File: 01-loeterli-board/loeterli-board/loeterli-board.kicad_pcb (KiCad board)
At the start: 2 copper layers, 100 x 60 mm, 45 parts, among them J5 Screw_Terminal_01x03, J8 Conn_01x03, Q1 PSMN5R2-60YL, SW1 SW_Push, SW2 SW_Push, SW3 SW_Push, SW4 SW_Push, U1 VOM1271T, U2 STM32F103C8Tx, U3 R-78HB3.3-0.5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

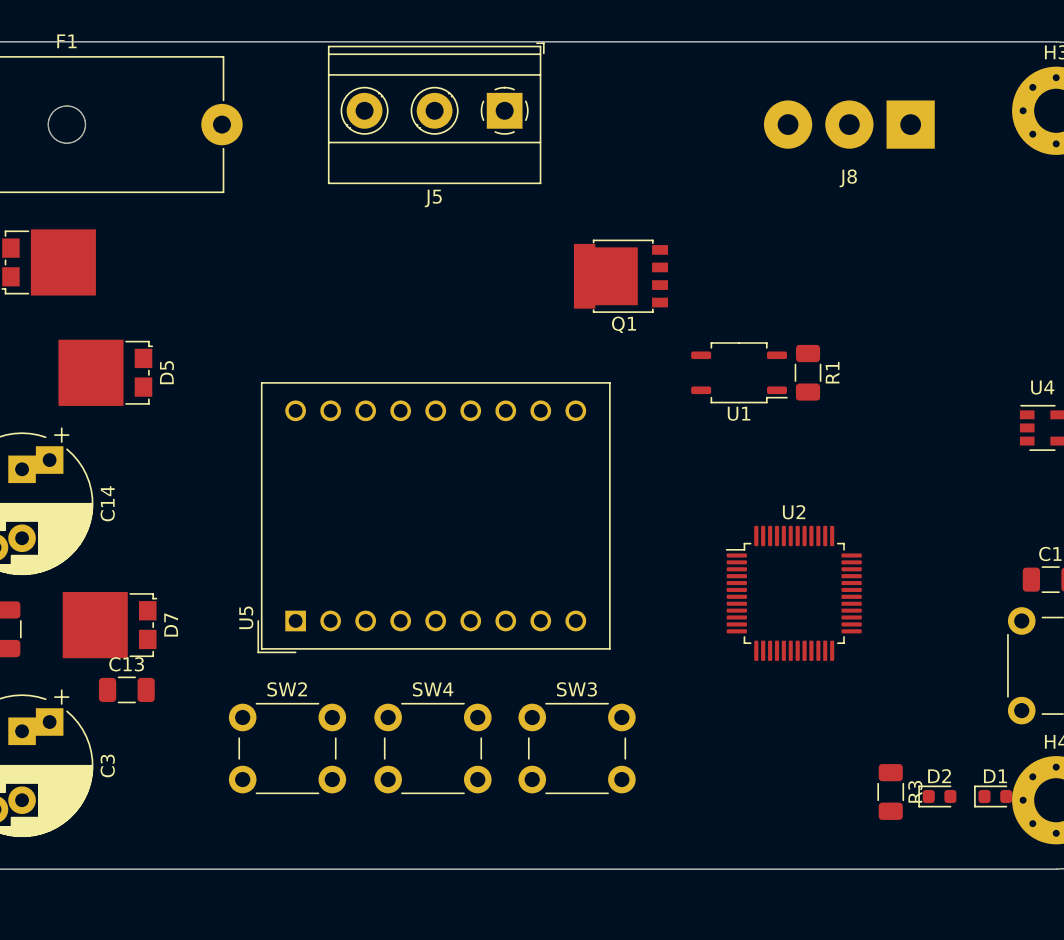
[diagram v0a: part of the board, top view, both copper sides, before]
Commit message: added readme image + misc
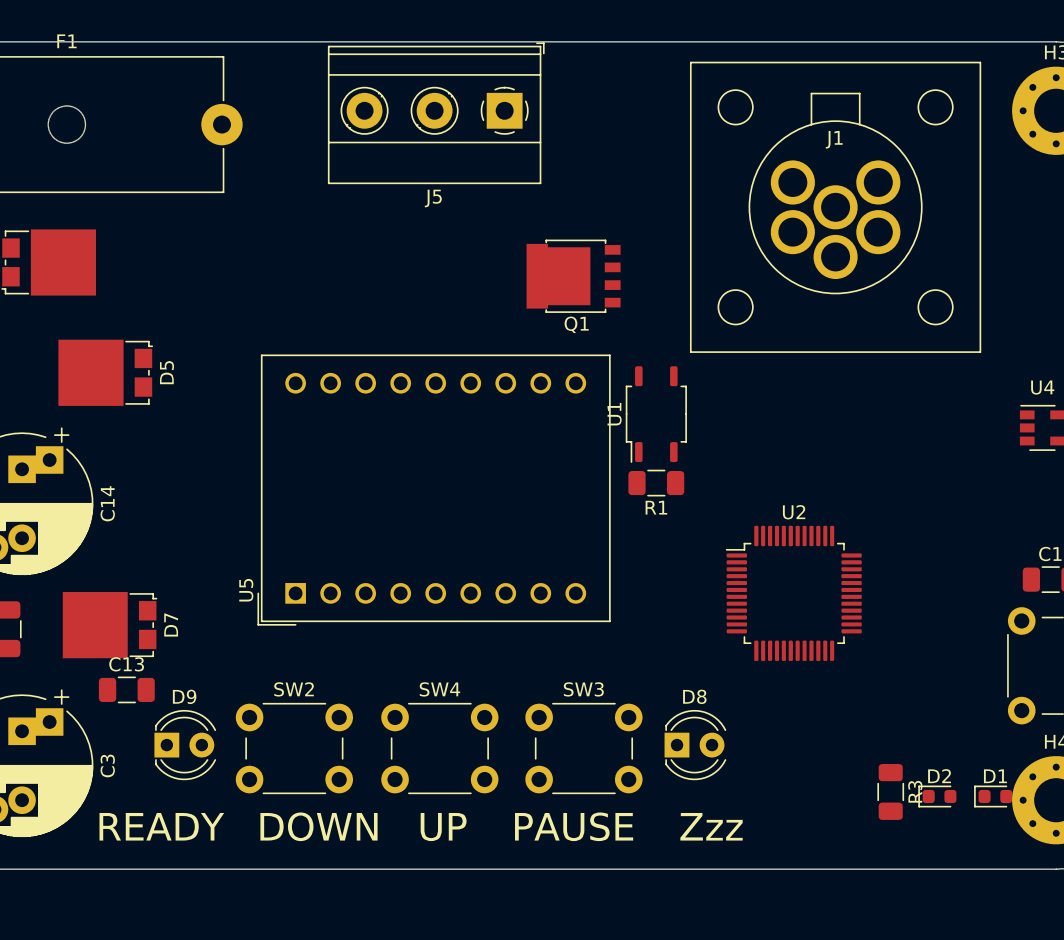
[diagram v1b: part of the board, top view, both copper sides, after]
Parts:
- removed J8: Conn_01x03, Connector_Wire:SolderWirePad_1x03_P4.445mm_Drill1.5mm
- added D8: LED, LED_THT:LED_D4.0mm, F.Cu at (187.5, 101.0)
- added D9: LED, LED_THT:LED_D4.0mm, F.Cu at (150.5, 101.0)
- added J1: RPC1-12RB-6P, loeterli:RPC1-12RB-6P, F.Cu at (199.0, 62.0)
- moved R1 13.6 mm to (186.0, 82.0), turned to 180 degrees
- moved U1 6.71 mm to (186.0, 77.0), turned to 90 degrees
- moved Q1 3.44 mm to (180.0, 67.0)
- moved U5 2.00 mm to (159.8, 90.0)
- moved SW2 0.50 mm to (156.5, 99.0)
- moved SW3 0.50 mm to (177.5, 99.0)
- moved SW4 0.50 mm to (167.1, 99.0)
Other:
- board text added: "DOWN"
- board text added: "PAUSE"
- board text added: "READY"
- board text added: "UP"
- board text added: "Zzz"

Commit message: misc
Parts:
- added D10: D, Diode_SMD:D_0603_1608Metric, F.Cu at (215.0, 119.5)
- added R7: 100k, Resistor_SMD:R_1206_3216Metric, F.Cu at (215.8, 116.6)
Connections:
- J1 pad 1: Net-(J1-Pad1) -> Earth
- J1 pad 2: Net-(J1-Pad2) -> GND
- J1 pad 5: Net-(J1-Pad5) -> H+
- Q1 pad 1: Net-(Q1-Pad1) -> H+
- Q1 pad 2: Net-(Q1-Pad1) -> H+
- Q1 pad 3: Net-(Q1-Pad1) -> H+
- U1 pad 3: Net-(Q1-Pad1) -> H+
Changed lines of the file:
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@@
     (tracks 0)
     (zones 0)
-    (modules 47)
-    (nets 91)
+    (modules 49)
+    (nets 89)
   )
   (page A4)
@@
   (net 78 V_RECT)
   (net 79 AC_N)
-  (net 80 "Net-(Q1-Pad1)")
-  (net 81 "Net-(J1-Pad3)")
-  (net 82 "Net-(J1-Pad6)")
-  (net 83 "Net-(J1-Pad5)")
-  (net 84 "Net-(J1-Pad4)")
-  (net 85 "Net-(J1-Pad2)")
-  (net 86 "Net-(J1-Pad1)")
-  (net 87 "Net-(D8-Pad2)")
-  (net 88 "Net-(D8-Pad1)")
-  (net 89 "Net-(D9-Pad2)")
-  (net 90 "Net-(D9-Pad1)")
+  (net 80 "Net-(J1-Pad3)")
+  (net 81 "Net-(J1-Pad6)")
+  (net 82 "Net-(J1-Pad4)")
+  (net 83 "Net-(D8-Pad2)")
+  (net 84 "Net-(D8-Pad1)")
+  (net 85 "Net-(D9-Pad2)")
+  (net 86 "Net-(D9-Pad1)")
+  (net 87 ZCD)
+  (net 88 H+)
   (net_class Default "This is the default net class."
     (clearance 0.2)
@@
     (add_net Earth)
     (add_net GND)
+    (add_net H+)
     (add_net "Net-(C1-Pad1)")
     (add_net "Net-(C11-Pad1)")
@@
     (add_net "Net-(D9-Pad2)")
     (add_net "Net-(F1-Pad2)")
-    (add_net "Net-(J1-Pad1)")
-    (add_net "Net-(J1-Pad2)")
     (add_net "Net-(J1-Pad3)")
     (add_net "Net-(J1-Pad4)")
-    (add_net "Net-(J1-Pad5)")
     (add_net "Net-(J1-Pad6)")
-    (add_net "Net-(Q1-Pad1)")
     (add_net "Net-(Q1-Pad4)")
     (add_net "Net-(R1-Pad2)")
@@
     (add_net TEMP)
     (add_net V_RECT)
+    (add_net ZCD)
     (add_net nGATE)
+  )
+  (module Resistor_SMD:R_1206_3216Metric (layer F.Cu)
+    (at 215.76 116.56)
+    (descr "Resistor SMD 1206 (3216 Metric), square (rectangular) end terminal, IPC_7351 nominal, (Body size source: http://www.tortai-tech.com/upload/download/2011102023233369053.pdf), generated with kicad-footprint-generator")
+    (tags resistor)
+    (attr smd)
+    (fp_text reference R7 (at 0 -1.82) (layer F.SilkS)
+      (effects (font (size 1 1) (thickness 0.15)))
+    )
+    (fp_text value 100k (at 0 1.82) (layer F.Fab)
+      (effects (font (size 1 1) (thickness 0.15)))
+    )
+    (fp_text user %R (at 0 0) (layer F.Fab)
+      (effects (font (size 0.8 0.8) (thickness 0.12)))
+    )
+    (fp_line (start 2.28 1.12) (end -2.28 1.12) (layer F.CrtYd) (width 0.05))
+    (fp_line (start 2.28 -1.12) (end 2.28 1.12) (layer F.CrtYd) (width 0.05))
+    (fp_line (start -2.28 -1.12) (end 2.28 -1.12) (layer F.CrtYd) (width 0.05))
+    (fp_line (start -2.28 1.12) (end -2.28 -1.12) (layer F.CrtYd) (width 0.05))
+    (fp_line (start -0.602064 0.91) (end 0.602064 0.91) (layer F.SilkS) (width 0.12))
+    (fp_line (start -0.602064 -0.91) (end 0.602064 -0.91) (layer F.SilkS) (width 0.12))
+    (fp_line (start 1.6 0.8) (end -1.6 0.8) (layer F.Fab) (width 0.1))
+    (fp_line (start 1.6 -0.8) (end 1.6 0.8) (layer F.Fab) (width 0.1))
+    (fp_line (start -1.6 -0.8) (end 1.6 -0.8) (layer F.Fab) (width 0.1))
+    (fp_line (start -1.6 0.8) (end -1.6 -0.8) (layer F.Fab) (width 0.1))
+    (pad 2 smd roundrect (at 1.4 0) (size 1.25 1.75) (layers F.Cu F.Paste F.Mask) (roundrect_rratio 0.2)
+      (net 87 ZCD))
+    (pad 1 smd roundrect (at -1.4 0) (size 1.25 1.75) (layers F.Cu F.Paste F.Mask) (roundrect_rratio 0.2)
+      (net 78 V_RECT))
+    (model ${KISYS3DMOD}/Resistor_SMD.3dshapes/R_1206_3216Metric.wrl
+      (at (xyz 0 0 0))
+      (scale (xyz 1 1 1))
+      (rotate (xyz 0 0 0))
+    )
+  )
+  (module Diode_SMD:D_0603_1608Metric (layer F.Cu)
+    (at 215 119.5)
+    (descr "Diode SMD 0603 (1608 Metric), square (rectangular) end terminal, IPC_7351 nominal, (Body size source: http://www.tortai-tech.com/upload/download/2011102023233369053.pdf), generated with kicad-footprint-generator")
+    (tags diode)
+    (attr smd)
+    (fp_text reference D10 (at 0 -1.43) (layer F.SilkS)
+      (effects (font (size 1 1) (thickness 0.15)))
+    )
+    (fp_text value D (at 0 1.43) (layer F.Fab)
+      (effects (font (size 1 1) (thickness 0.15)))
+    )
+    (fp_text user %R (at 0 0) (layer F.Fab)
+      (effects (font (size 0.4 0.4) (thickness 0.06)))
+    )
+    (fp_line (start 1.48 0.73) (end -1.48 0.73) (layer F.CrtYd) (width 0.05))
+    (fp_line (start 1.48 -0.73) (end 1.48 0.73) (layer F.CrtYd) (width 0.05))
+    (fp_line (start -1.48 -0.73) (end 1.48 -0.73) (layer F.CrtYd) (width 0.05))
+    (fp_line (start -1.48 0.73) (end -1.48 -0.73) (layer F.CrtYd) (width 0.05))
+    (fp_line (start -1.485 0.735) (end 0.8 0.735) (layer F.SilkS) (width 0.12))
+    (fp_line (start -1.485 -0.735) (end -1.485 0.735) (layer F.SilkS) (width 0.12))
+    (fp_line (start 0.8 -0.735) (end -1.485 -0.735) (layer F.SilkS) (width 0.12))
+    (fp_line (start 0.8 0.4) (end 0.8 -0.4) (layer F.Fab) (width 0.1))
+    (fp_line (start -0.8 0.4) (end 0.8 0.4) (layer F.Fab) (width 0.1))
+    (fp_line (start -0.8 -0.1) (end -0.8 0.4) (layer F.Fab) (width 0.1))
+    (fp_line (start -0.5 -0.4) (end -0.8 -0.1) (layer F.Fab) (width 0.1))
+    (fp_line (start 0.8 -0.4) (end -0.5 -0.4) (layer F.Fab) (width 0.1))
+    (pad 2 smd roundrect (at 0.7875 0) (size 0.875 0.95) (layers F.Cu F.Paste F.Mask) (roundrect_rratio 0.25)
+      (net 87 ZCD))
+    (pad 1 smd roundrect (at -0.7875 0) (size 0.875 0.95) (layers F.Cu F.Paste F.Mask) (roundrect_rratio 0.25)
+      (net 3 +3V3))
+    (model ${KISYS3DMOD}/Diode_SMD.3dshapes/D_0603_1608Metric.wrl
+      (at (xyz 0 0 0))
+      (scale (xyz 1 1 1))
+      (rotate (xyz 0 0 0))
+    )
   )
   (module LED_THT:LED_D4.0mm (layer F.Cu)
@@
     (fp_arc (start 1.27 0) (end -0.73 -1.32665) (angle 292.9) (layer F.Fab) (width 0.1))
     (pad 2 thru_hole circle (at 2.54 0) (size 1.8 1.8) (drill 0.9) (layers *.Cu *.Mask)
-      (net 89 "Net-(D9-Pad2)"))
+      (net 85 "Net-(D9-Pad2)"))
     (pad 1 thru_hole rect (at 0 0) (size 1.8 1.8) (drill 0.9) (layers *.Cu *.Mask)
-      (net 90 "Net-(D9-Pad1)"))
+      (net 86 "Net-(D9-Pad1)"))
     (model ${KISYS3DMOD}/LED_THT.3dshapes/LED_D4.0mm.wrl
       (at (xyz 0 0 0))
@@
     (fp_arc (start 1.27 0) (end -0.73 -1.32665) (angle 292.9) (layer F.Fab) (width 0.1))
     (pad 2 thru_hole circle (at 2.54 0) (size 1.8 1.8) (drill 0.9) (layers *.Cu *.Mask)
-      (net 87 "Net-(D8-Pad2)"))
+      (net 83 "Net-(D8-Pad2)"))
     (pad 1 thru_hole rect (at 0 0) (size 1.8 1.8) (drill 0.9) (layers *.Cu *.Mask)
-      (net 88 "Net-(D8-Pad1)"))
+      (net 84 "Net-(D8-Pad1)"))
     (model ${KISYS3DMOD}/LED_THT.3dshapes/LED_D4.0mm.wrl
       (at (xyz 0 0 0))
@@
     (fp_line (start -11 -11) (end 11 -11) (layer F.CrtYd) (width 0.12))
     (pad 3 thru_hole circle (at 0 3.6 180) (size 3.2 3.2) (drill 2.1) (layers *.Cu *.Mask)
-      (net 81 "Net-(J1-Pad3)"))
+      (net 80 "Net-(J1-Pad3)"))
     (pad 6 thru_hole circle (at 0 0 180) (size 3.2 3.2) (drill 2.1) (layers *.Cu *.Mask)
-      (net 82 "Net-(J1-Pad6)"))
+      (net 81 "Net-(J1-Pad6)"))
     (pad 5 thru_hole circle (at 3.1 -1.8 180) (size 3.2 3.2) (drill 2.1) (layers *.Cu *.Mask)
-      (net 83 "Net-(J1-Pad5)"))
+      (net 88 H+))
     (pad 4 thru_hole circle (at 3.1 1.8 180) (size 3.2 3.2) (drill 2.1) (layers *.Cu *.Mask)
-      (net 84 "Net-(J1-Pad4)"))
+      (net 82 "Net-(J1-Pad4)"))
     (pad 2 thru_hole circle (at -3.1 1.8) (size 3.2 3.2) (drill 2.1) (layers *.Cu *.Mask)
-      (net 85 "Net-(J1-Pad2)"))
+      (net 1 GND))
     (pad 1 thru_hole circle (at -3.1 -1.8) (size 3.2 3.2) (drill 2.1) (layers *.Cu *.Mask)
-      (net 86 "Net-(J1-Pad1)"))
+      (net 75 Earth))
     (model ../../00-kicad-lib/loeterli-3d/RPC1-12RB-6P.step
       (offset (xyz 0 0 6.2))
@@
       (net 74 "Net-(Q1-Pad4)") (solder_mask_margin 0.07) (solder_paste_margin -0.05))
     (pad 3 smd rect (at -2.835 0.64 90) (size 0.7 1.15) (layers F.Cu F.Paste F.Mask)
-      (net 80 "Net-(Q1-Pad1)") (solder_mask_margin 0.07) (solder_paste_margin -0.05))
+      (net 88 H+) (solder_mask_margin 0.07) (solder_paste_margin -0.05))
     (pad 1 smd rect (at -2.835 -1.91 90) (size 0.7 1.15) (layers F.Cu F.Paste F.Mask)
-      (net 80 "Net-(Q1-Pad1)") (solder_mask_margin 0.07) (solder_paste_margin -0.05))
+      (net 88 H+) (solder_mask_margin 0.07) (solder_paste_margin -0.05))
     (pad 2 smd rect (at -2.835 -0.64 90) (size 0.7 1.15) (layers F.Cu F.Paste F.Mask)
-      (net 80 "Net-(Q1-Pad1)") (solder_mask_margin 0.07) (solder_paste_margin -0.05))
+      (net 88 H+) (solder_mask_margin 0.07) (solder_paste_margin -0.05))
     (pad "" smd rect (at 2.885 -0.6 90) (size 0.6 0.9) (layers F.Paste))
     (pad "" smd rect (at 2.885 1.88 90) (size 0.6 0.9) (layers F.Paste))
@@
       (net 74 "Net-(Q1-Pad4)"))
     (pad 3 smd roundrect (at 2.75 1.27 90) (size 1.45 0.55) (layers F.Cu F.Paste F.Mask) (roundrect_rratio 0.25)
-      (net 80 "Net-(Q1-Pad1)"))
+      (net 88 H+))
     (pad 2 smd roundrect (at -2.75 1.27 90) (size 1.45 0.55) (layers F.Cu F.Paste F.Mask) (roundrect_rratio 0.25)
       (net 12 nGATE))

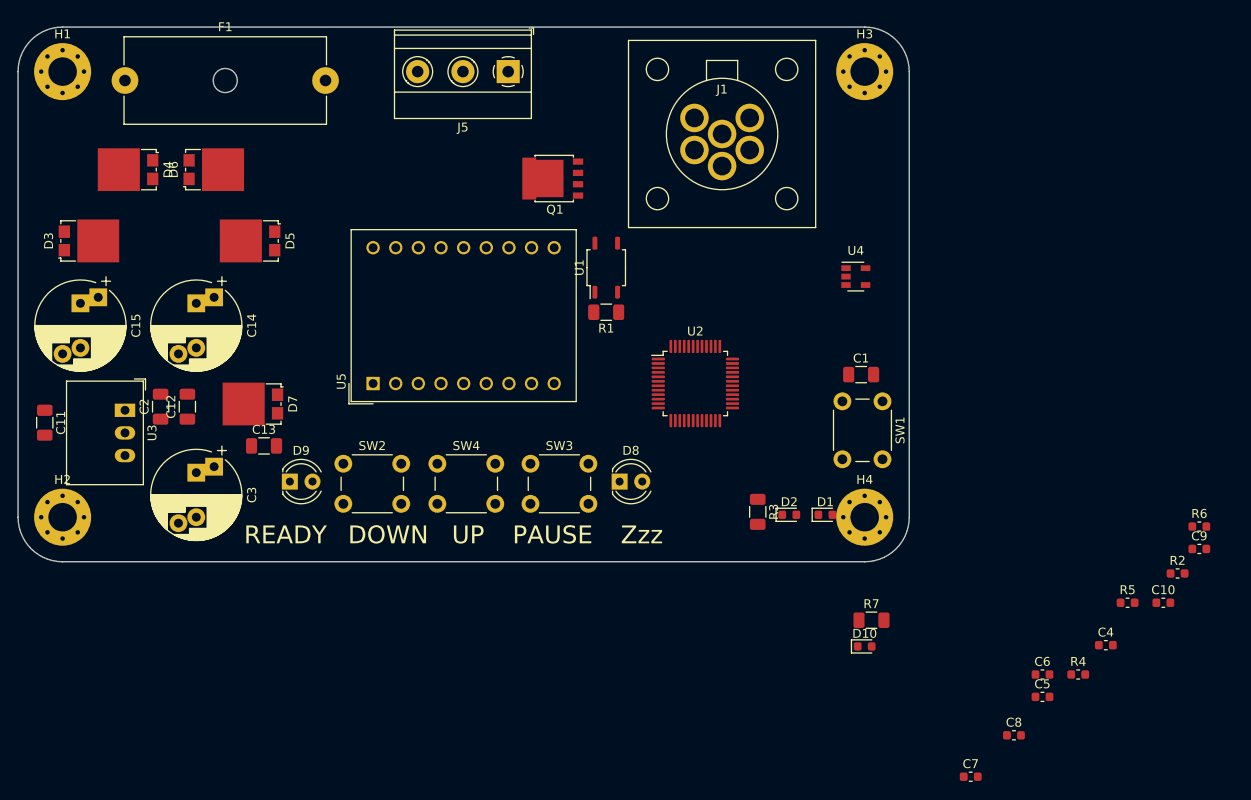
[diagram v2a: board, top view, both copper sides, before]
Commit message: changed tc amp
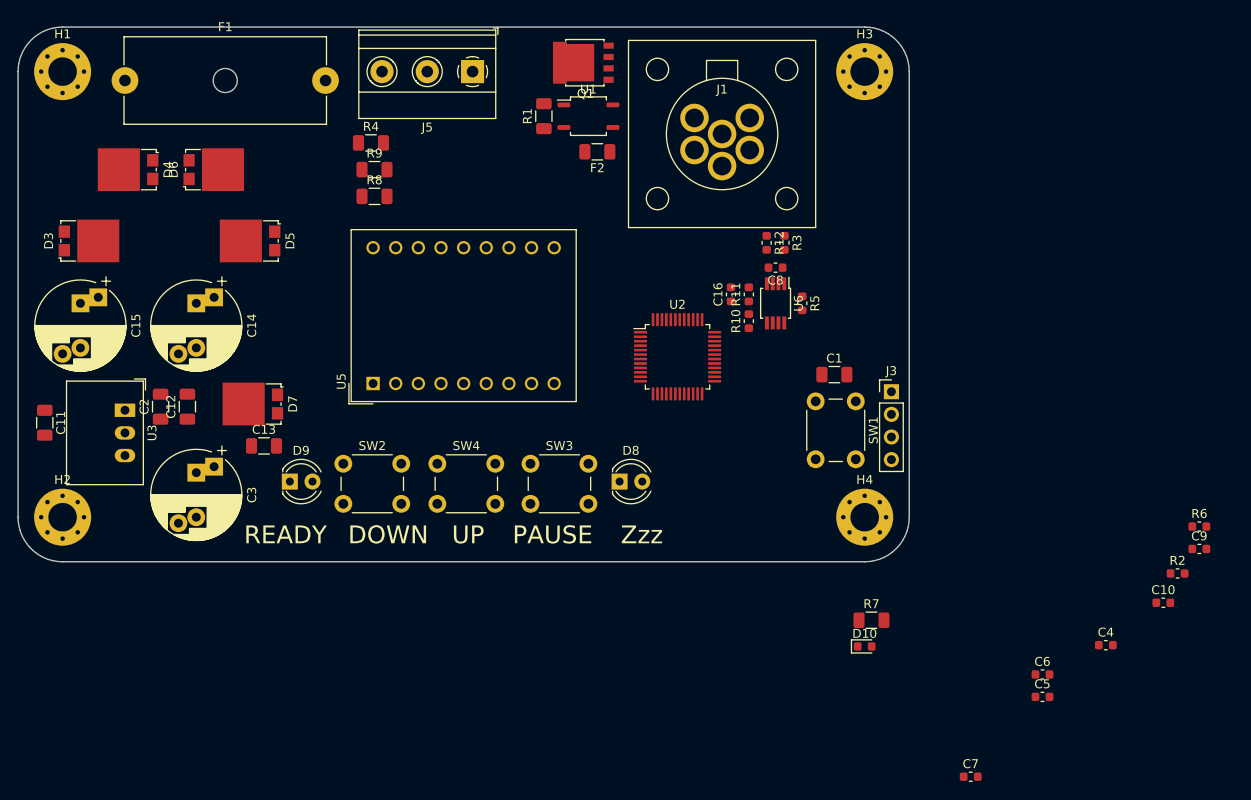
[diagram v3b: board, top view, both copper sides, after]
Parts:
- removed D1, D2: D, Diode_SMD:D_0603_1608Metric
- removed U4: TSZ121, Package_TO_SOT_SMD:SOT-23-5
- added C16: C, Capacitor_SMD:C_0603_1608Metric, F.Cu at (200.0, 80.0)
- added F2: Fuse, Fuse:Fuse_1206_3216Metric, F.Cu at (185.0, 64.0)
- added J3: Conn_01x04, Connector_PinHeader_2.54mm:PinHeader_1x04_P2.54mm_Vertical, F.Cu at (218.0, 90.9)
- added R10: 1k, Resistor_SMD:R_0603_1608Metric, F.Cu at (202.0, 83.0)
- added R11: 1k, Resistor_SMD:R_0603_1608Metric, F.Cu at (202.0, 80.0)
- added R12: 100, Resistor_SMD:R_0603_1608Metric, F.Cu at (204.0, 74.2)
- added R8: 100k, Resistor_SMD:R_1206_3216Metric, F.Cu at (160.0, 69.0)
- added R9: 100k, Resistor_SMD:R_1206_3216Metric, F.Cu at (160.0, 66.0)
- added U6: AD8227, Package_SO:MSOP-8_3x3mm_P0.65mm, F.Cu at (205.0, 81.0)
- R3: value 10k -> 100; footprint Resistor_SMD:R_1206_3216Metric -> Resistor_SMD:R_0603_1608Metric
- R4: value R -> 100k; footprint Resistor_SMD:R_0603_1608Metric -> Resistor_SMD:R_1206_3216Metric
- R5: value R -> 845
- moved R4 99.3 mm to (159.6, 63.0)
- moved C8 58.9 mm to (205.0, 77.0), turned to 180 degrees
- moved R5 49.6 mm to (208.0, 81.0), turned to 270 degrees
- moved R3 30.3 mm to (206.0, 74.2)
- moved R1 23.1 mm to (179.0, 60.0), turned to 90 degrees
- moved U1 17.1 mm to (184.0, 60.0), turned to 0 degrees
- moved Q1 13.4 mm to (183.4, 54.0)
- moved J5 4.00 mm to (171.0, 55.0)
- moved U2 3.61 mm to (194.0, 87.0)
- moved C1 3.00 mm to (211.6, 89.0)
- moved SW1 3.00 mm to (214.0, 92.0)
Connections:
- C8 pad 2: GND -> Net-(C8-Pad2)
- J1 pad 1: Earth -> TC_EARTH
- J1 pad 2: GND -> H-
- R3 pad 1: Net-(R3-Pad1) -> TC_EARTH
- R4 pad 1: Net-(R4-Pad1) -> GND
- R4 pad 2: Net-(R4-Pad2) -> H-
- R5 pad 1: GND -> Net-(R5-Pad1)
- R5 pad 2: Net-(R4-Pad1) -> Net-(R5-Pad2)
- R6 pad 1: Net-(R4-Pad2) -> Net-(R6-Pad1)
